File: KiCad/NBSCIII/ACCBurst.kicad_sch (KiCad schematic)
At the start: 56 parts, among them Q901 BC337-25, Q902 BC337-25, Q903 BC337-25, Q910 BC337-25, Q911 BC337-25, Q912 BC337-25, U1 LM324N

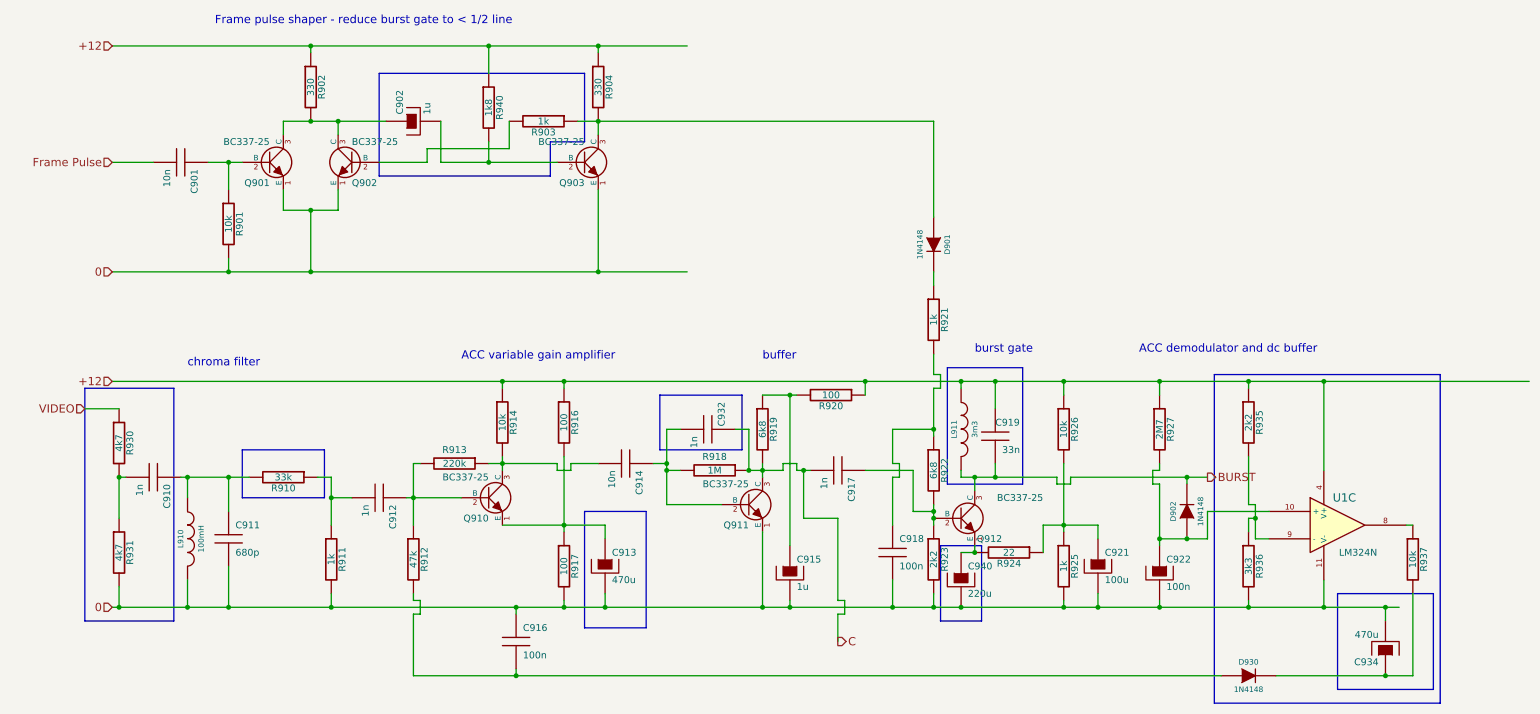
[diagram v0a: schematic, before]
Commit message: unrescue to Device:C
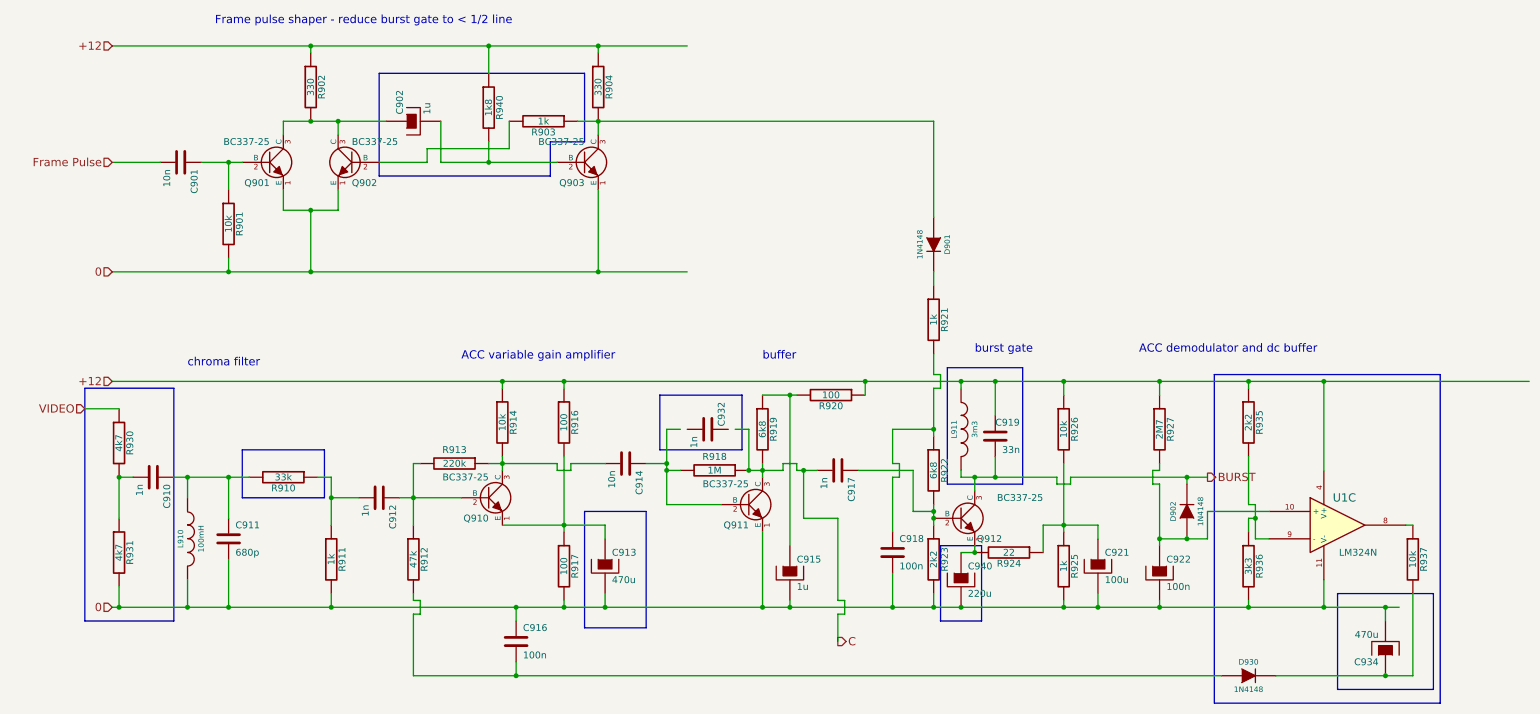
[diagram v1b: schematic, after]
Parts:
- C901, C910, C911, C912, C914, C916, C917, C918, C919, C932: symbol NBSCIII-rescue:C -> Device:C
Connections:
- net C: no longer C932.1
- net at C914.1, Q911.2 (B), R918.2: no longer C932.2
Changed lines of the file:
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@@
     (stroke (width 0) (type default) (color 0 0 0 0))
   )
-  (wire (pts (xy 176.53 104.14) (xy 167.64 104.14))
+  (wire (pts (xy 166.37 104.14) (xy 176.53 104.14))
     (stroke (width 0) (type default) (color 0 0 0 0))
   )
@@
     (stroke (width 0) (type default) (color 0 0 0 0))
   )
-  (wire (pts (xy 102.87 142.24) (xy 102.87 140.97))
+  (wire (pts (xy 102.87 139.7) (xy 102.87 142.24))
     (stroke (width 0) (type default) (color 0 0 0 0))
   )
@@
     (stroke (width 0) (type default) (color 0 0 0 0))
   )
-  (wire (pts (xy 72.39 109.22) (xy 68.58 109.22))
+  (wire (pts (xy 39.37 105.41) (xy 41.91 105.41))
+    (stroke (width 0) (type default) (color 0 0 0 0))
+  )
+  (wire (pts (xy 68.58 109.22) (xy 73.66 109.22))
     (stroke (width 0) (type default) (color 0 0 0 0))
   )
@@
     (stroke (width 0) (type default) (color 0 0 0 0))
   )
-  (wire (pts (xy 172.72 129.54) (xy 172.72 124.46))
-    (stroke (width 0) (type default) (color 0 0 0 0))
-  )
   (wire (pts (xy 210.82 129.54) (xy 210.82 127))
     (stroke (width 0) (type default) (color 0 0 0 0))
@@
     (stroke (width 0) (type default) (color 0 0 0 0))
   )
-  (wire (pts (xy 118.11 102.87) (xy 113.03 102.87))
+  (wire (pts (xy 113.03 102.87) (xy 119.38 102.87))
     (stroke (width 0) (type default) (color 0 0 0 0))
   )
@@
     (stroke (width 0) (type default) (color 0 0 0 0))
   )
-  (wire (pts (xy 49.53 105.41) (xy 49.53 111.76))
+  (wire (pts (xy 49.53 105.41) (xy 49.53 113.03))
     (stroke (width 0) (type default) (color 0 0 0 0))
   )
@@
     (stroke (width 0) (type default) (color 0 0 0 0))
   )
+  (wire (pts (xy 102.87 129.54) (xy 102.87 132.08))
+    (stroke (width 0) (type default) (color 0 0 0 0))
+  )
   (wire (pts (xy 118.11 67.31) (xy 134.62 67.31))
     (stroke (width 0) (type default) (color 0 0 0 0))
@@
     (stroke (width 0) (type default) (color 0 0 0 0))
   )
+  (wire (pts (xy 172.72 123.19) (xy 172.72 129.54))
+    (stroke (width 0) (type default) (color 0 0 0 0))
+  )
   (wire (pts (xy 180.34 129.54) (xy 180.34 127))
     (stroke (width 0) (type default) (color 0 0 0 0))
@@
     (stroke (width 0) (type default) (color 0 0 0 0))
   )
-  (wire (pts (xy 29.21 105.41) (xy 30.48 105.41))
+  (wire (pts (xy 29.21 105.41) (xy 31.75 105.41))
     (stroke (width 0) (type default) (color 0 0 0 0))
   )
@@
     (stroke (width 0) (type default) (color 0 0 0 0))
   )
-  (wire (pts (xy 102.87 129.54) (xy 102.87 130.81))
-    (stroke (width 0) (type default) (color 0 0 0 0))
-  )
   (polyline (pts (xy 129.54 90.17) (xy 144.78 90.17))
     (stroke (width 0) (type default) (color 0 0 0 0))
@@
     (stroke (width 0) (type default) (color 0 0 0 0))
   )
-  (wire (pts (xy 40.64 105.41) (xy 41.91 105.41))
-    (stroke (width 0) (type default) (color 0 0 0 0))
-  )
   (wire (pts (xy 110.49 104.14) (xy 110.49 102.87))
     (stroke (width 0) (type default) (color 0 0 0 0))
@@
     (stroke (width 0) (type default) (color 0 0 0 0))
   )
-  (wire (pts (xy 191.77 105.41) (xy 191.77 102.87))
+  (wire (pts (xy 191.77 101.6) (xy 191.77 105.41))
     (stroke (width 0) (type default) (color 0 0 0 0))
   )
@@
     (stroke (width 0) (type default) (color 0 0 0 0))
   )
-  (wire (pts (xy 156.21 104.14) (xy 157.48 104.14))
+  (wire (pts (xy 156.21 104.14) (xy 158.75 104.14))
     (stroke (width 0) (type default) (color 0 0 0 0))
   )
@@
     (stroke (width 0) (type default) (color 0 0 0 0))
   )
-  (wire (pts (xy 82.55 109.22) (xy 83.82 109.22))
+  (wire (pts (xy 81.28 109.22) (xy 83.82 109.22))
     (stroke (width 0) (type default) (color 0 0 0 0))
   )
@@
     (stroke (width 0) (type default) (color 0 0 0 0))
   )
-  (wire (pts (xy 172.72 105.41) (xy 172.72 114.3))
+  (wire (pts (xy 172.72 105.41) (xy 172.72 115.57))
     (stroke (width 0) (type default) (color 0 0 0 0))
   )
@@
     (stroke (width 0) (type default) (color 0 0 0 0))
   )
-  (wire (pts (xy 49.53 129.54) (xy 49.53 121.92))
+  (wire (pts (xy 49.53 120.65) (xy 49.53 129.54))
     (stroke (width 0) (type default) (color 0 0 0 0))
   )
@@
     (stroke (width 0) (type default) (color 0 0 0 0))
   )
-  (wire (pts (xy 191.77 87.63) (xy 191.77 92.71))
+  (wire (pts (xy 191.77 87.63) (xy 191.77 93.98))
     (stroke (width 0) (type default) (color 0 0 0 0))
   )
@@
     (stroke (width 0) (type default) (color 0 0 0 0))
   )
-  (wire (pts (xy 130.81 102.87) (xy 128.27 102.87))
+  (wire (pts (xy 127 102.87) (xy 130.81 102.87))
     (stroke (width 0) (type default) (color 0 0 0 0))
   )
@@
     (stroke (width 0) (type default) (color 0 0 0 0))
   )
-  (wire (pts (xy 35.56 46.99) (xy 27.94 46.99))
+  (wire (pts (xy 27.94 46.99) (xy 36.83 46.99))
     (stroke (width 0) (type default) (color 0 0 0 0))
   )
@@
     (stroke (width 0) (type default) (color 0 0 0 0))
   )
-  (wire (pts (xy 49.53 46.99) (xy 45.72 46.99))
+  (wire (pts (xy 44.45 46.99) (xy 49.53 46.99))
     (stroke (width 0) (type default) (color 0 0 0 0))
   )
@@
     (pin "2")
   )
-  (symbol (lib_id "NBSCIII-rescue:C") (at 40.64 46.99 270) (unit 1)
+  (symbol (lib_id "Device:C") (at 40.64 46.99 270) (unit 1)
     (in_bom yes) (on_board yes)
     (property "Reference" "C901" (id 0) (at 43.18 48.26 0)
@@
     (pin "2")
   )
-  (symbol (lib_id "NBSCIII-rescue:C") (at 49.53 116.84 0) (unit 1)
+  (symbol (lib_id "Device:C") (at 49.53 116.84 0) (unit 1)
     (in_bom yes) (on_board yes)
     (property "Reference" "C911" (id 0) (at 50.8 114.3 0)
@@
     (pin "2")
   )
-  (symbol (lib_id "NBSCIII-rescue:C") (at 77.47 109.22 270) (unit 1)
+  (symbol (lib_id "Device:C") (at 77.47 109.22 270) (unit 1)
     (in_bom yes) (on_board yes)
     (property "Reference" "C912" (id 0) (at 80.01 110.49 0)
@@
     (pin "2")
   )
-  (symbol (lib_id "NBSCIII-rescue:C") (at 102.87 135.89 0) (unit 1)
+  (symbol (lib_id "Device:C") (at 102.87 135.89 0) (unit 1)
     (in_bom yes) (on_board yes)
     (property "Reference" "C916" (id 0) (at 104.14 133.35 0)
@@
     (pin "2")
   )
-  (symbol (lib_id "NBSCIII-rescue:C") (at 123.19 102.87 270) (unit 1)
+  (symbol (lib_id "Device:C") (at 123.19 102.87 270) (unit 1)
     (in_bom yes) (on_board yes)
     (property "Reference" "C914" (id 0) (at 125.73 104.14 0)
@@
     (pin "2")
   )
-  (symbol (lib_id "NBSCIII-rescue:C") (at 172.72 119.38 0) (unit 1)
+  (symbol (lib_id "Device:C") (at 172.72 119.38 0) (unit 1)
     (in_bom yes) (on_board yes)
     (property "Reference" "C918" (id 0) (at 173.99 116.84 0)
@@
     (pin "2")
   )
-  (symbol (lib_id "NBSCIII-rescue:C") (at 162.56 104.14 270) (unit 1)
+  (symbol (lib_id "Device:C") (at 162.56 104.14 270) (unit 1)
     (in_bom yes) (on_board yes)
     (property "Reference" "C917" (id 0) (at 165.1 105.41 0)
@@
     (pin "2")
   )
-  (symbol (lib_id "NBSCIII-rescue:C") (at 191.77 97.79 0) (unit 1)
+  (symbol (lib_id "Device:C") (at 191.77 97.79 0) (unit 1)
     (in_bom yes) (on_board yes)
     (property "Reference" "C919" (id 0) (at 191.77 95.25 0)
@@
     (pin "2")
   )
-  (symbol (lib_id "NBSCIII-rescue:C") (at 35.56 105.41 270) (unit 1)
+  (symbol (lib_id "Device:C") (at 35.56 105.41 270) (unit 1)
     (in_bom yes) (on_board yes)
     (property "Reference" "C910" (id 0) (at 38.1 106.68 0)
@@
     (pin "2")
   )
-  (symbol (lib_id "NBSCIII-rescue:C") (at 138.43 96.52 270) (unit 1)
+  (symbol (lib_id "Device:C") (at 138.43 96.52 270) (unit 1)
     (in_bom yes) (on_board yes)
     (property "Reference" "C932" (id 0) (at 140.97 91.44 0)

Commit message: unrescue to Device:C_Polarized
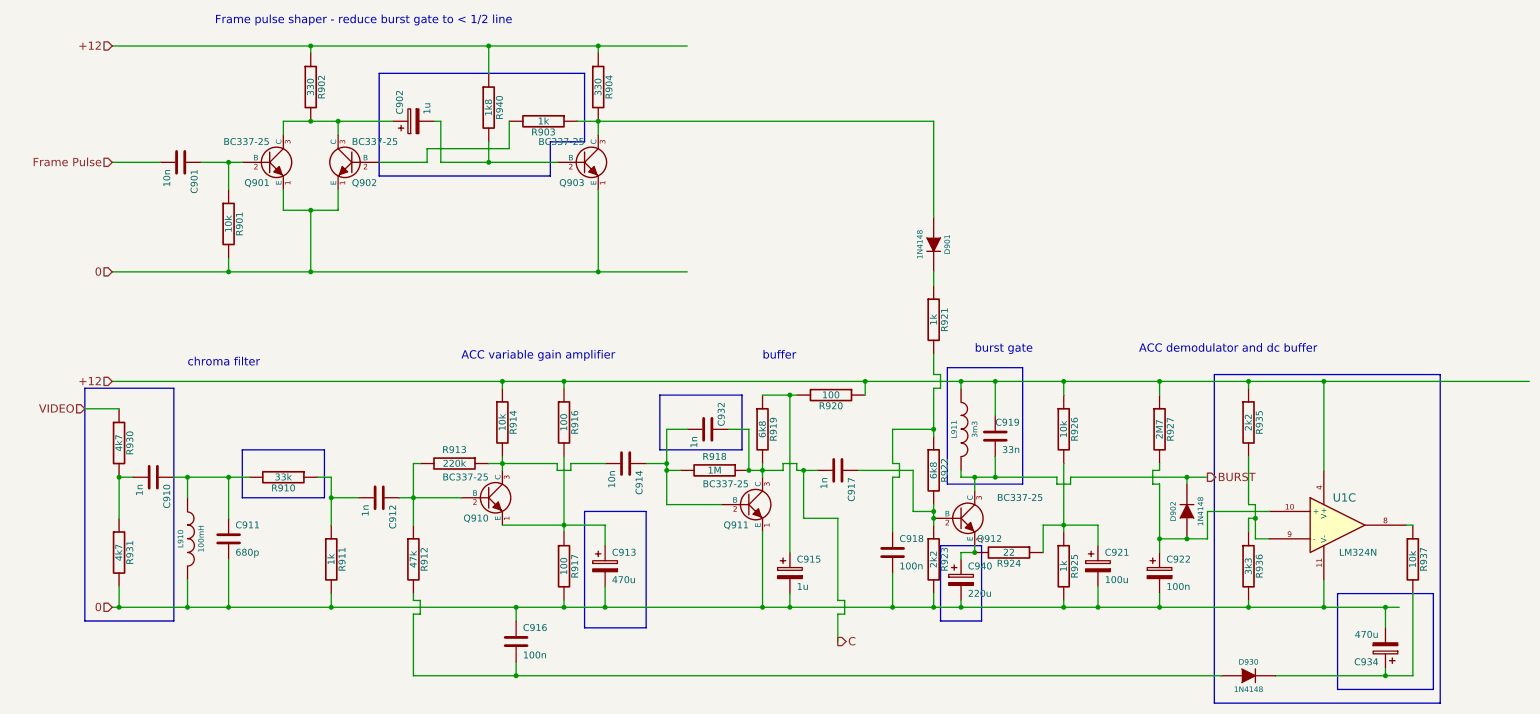
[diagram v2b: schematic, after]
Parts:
- C902, C913, C915, C921, C922, C934, C940: symbol NBSCIII-rescue:CP -> Device:C_Polarized
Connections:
- net C: now also C932.1
- net at C914.1, Q911.2 (B), R918.2: now also C932.2

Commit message: unrescue Device:R
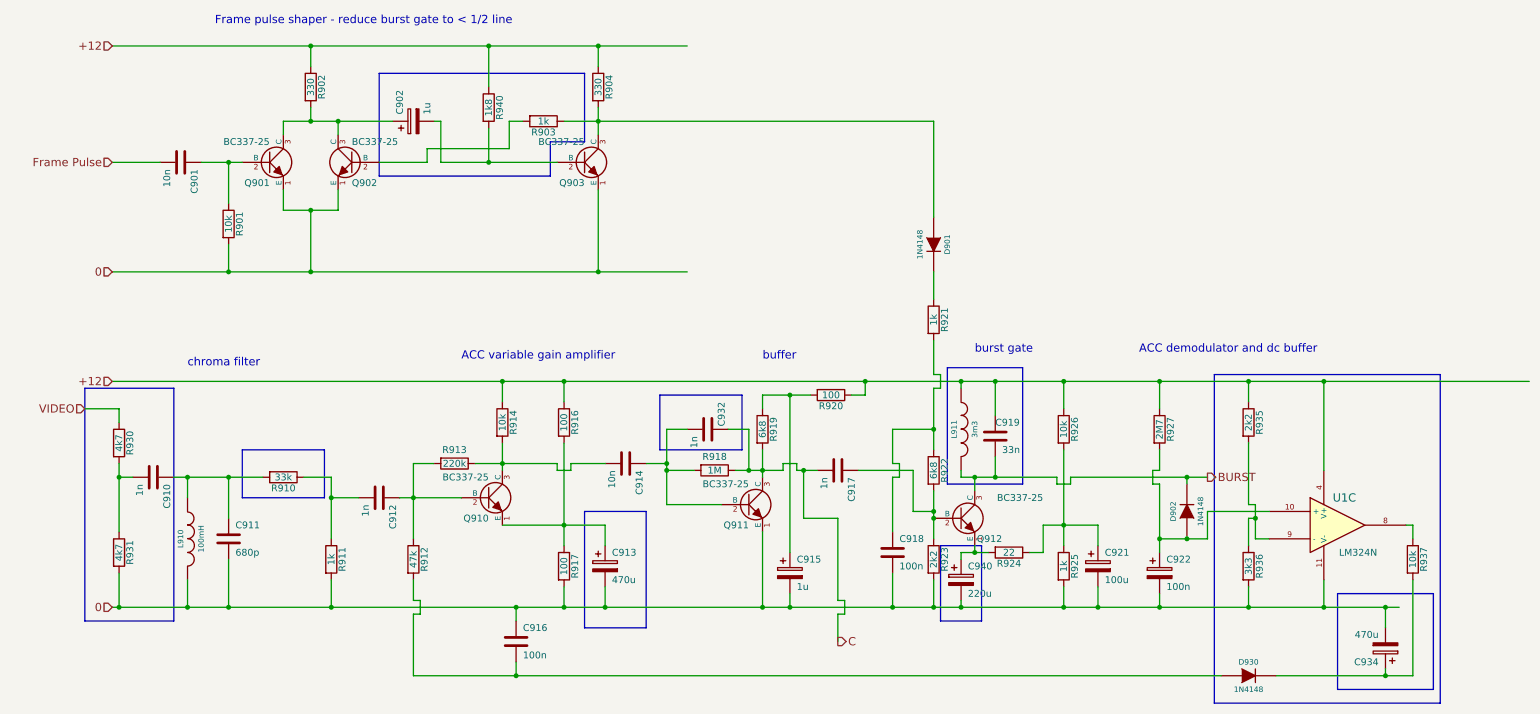
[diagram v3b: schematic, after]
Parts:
- R901, R902, R903, R904, R910, R911, R912, R913, R914, R916, R917, R918, R919, R920, R921, R922, R923, R924, R925, R926, R927, R930, R931, R935, R936, R937, R940: symbol NBSCIII-rescue:R -> Device:R

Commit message: unrescue NPN
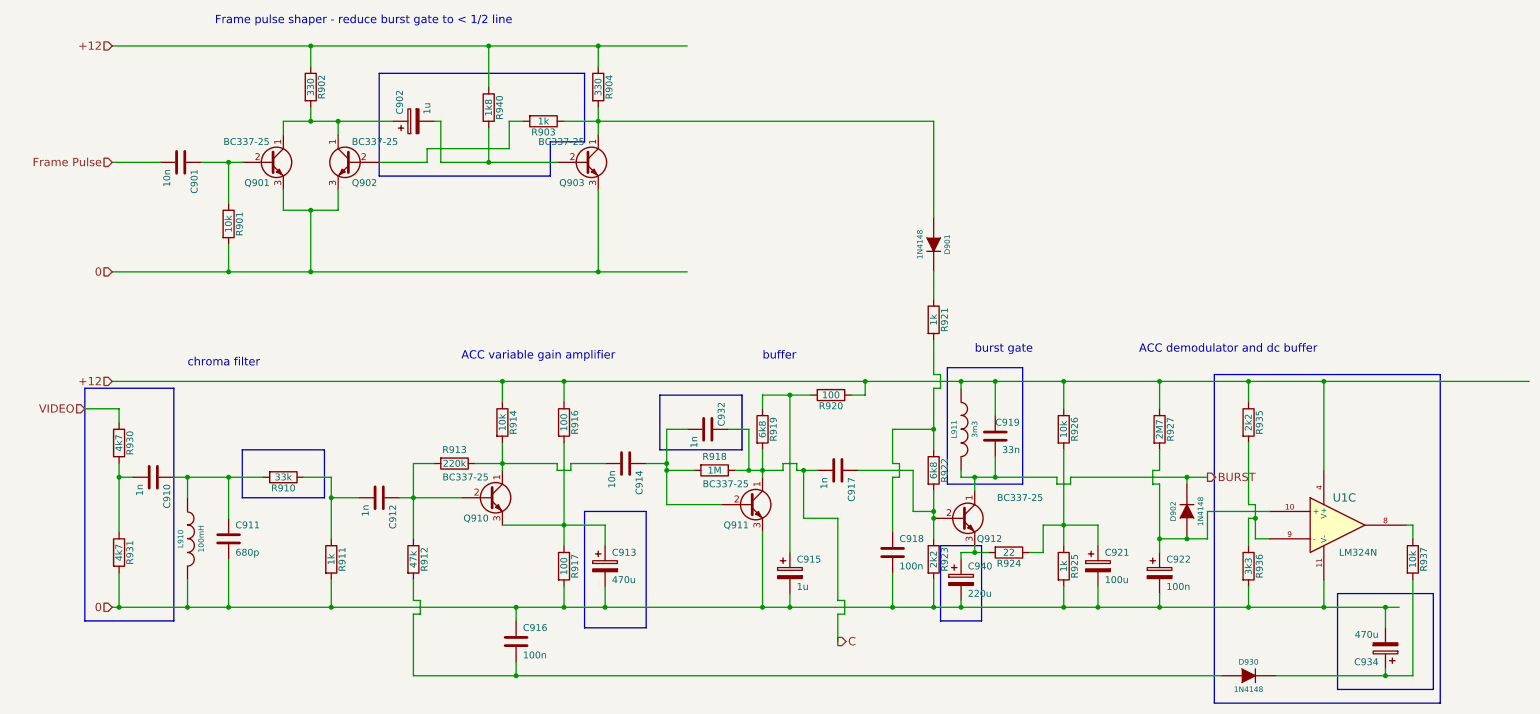
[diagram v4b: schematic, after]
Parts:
- Q901, Q902, Q903, Q910, Q911, Q912: symbol NBSCIII-rescue:NPN -> Device:Q_NPN_CBE
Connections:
- net 0: now also Q901.3 (E), Q902.3 (E), Q903.3 (E), Q911.3 (E); no longer Q901.1 (E), Q902.1 (E), Q903.1 (E), Q911.1 (E)
- net BURST: now also Q912.1 (C); no longer Q912.3 (C)
- net C: now also Q911.1 (C); no longer Q911.3 (C)
- net at C902.1, R902.2: now also Q901.1 (C), Q902.1 (C); no longer Q901.3 (C), Q902.3 (C)
- net at D901.1 (A), R903.1, R904.2: now also Q903.1 (C); no longer Q903.3 (C)
- net at C914.2, R913.1, R914.2: now also Q910.1 (C); no longer Q910.3 (C)
- net at C913.1, R916.2, R917.1: now also Q910.3 (E); no longer Q910.1 (E)
- net at C940.1, R924.2: now also Q912.3 (E); no longer Q912.1 (E)
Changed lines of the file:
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@@
     (effects (font (size 1.524 1.524)) (justify right))
   )
-  (symbol (lib_id "NBSCIII-rescue:NPN") (at 57.15 46.99 0) (unit 1)
+  (symbol (lib_id "Device:Q_NPN_CBE") (at 57.15 46.99 0) (unit 1)
     (in_bom yes) (on_board yes)
     (property "Reference" "Q901" (id 0) (at 57.15 50.8 0)
@@
     (pin "3")
   )
-  (symbol (lib_id "NBSCIII-rescue:NPN") (at 72.39 46.99 0) (mirror y) (unit 1)
+  (symbol (lib_id "Device:Q_NPN_CBE") (at 72.39 46.99 0) (mirror y) (unit 1)
     (in_bom yes) (on_board yes)
     (property "Reference" "Q902" (id 0) (at 72.39 50.8 0)
@@
     (pin "3")
   )
-  (symbol (lib_id "NBSCIII-rescue:NPN") (at 115.57 46.99 0) (unit 1)
+  (symbol (lib_id "Device:Q_NPN_CBE") (at 115.57 46.99 0) (unit 1)
     (in_bom yes) (on_board yes)
     (property "Reference" "Q903" (id 0) (at 115.57 50.8 0)
@@
     (pin "2")
   )
-  (symbol (lib_id "NBSCIII-rescue:NPN") (at 97.79 109.22 0) (unit 1)
+  (symbol (lib_id "Device:Q_NPN_CBE") (at 97.79 109.22 0) (unit 1)
     (in_bom yes) (on_board yes)
     (property "Reference" "Q910" (id 0) (at 97.79 113.03 0)
@@
     (pin "2")
   )
-  (symbol (lib_id "NBSCIII-rescue:NPN") (at 146.05 110.49 0) (unit 1)
+  (symbol (lib_id "Device:Q_NPN_CBE") (at 146.05 110.49 0) (unit 1)
     (in_bom yes) (on_board yes)
     (property "Reference" "Q911" (id 0) (at 146.05 114.3 0)
@@
     (pin "2")
   )
-  (symbol (lib_id "NBSCIII-rescue:NPN") (at 185.42 113.03 0) (unit 1)
+  (symbol (lib_id "Device:Q_NPN_CBE") (at 185.42 113.03 0) (unit 1)
     (in_bom yes) (on_board yes)
     (property "Reference" "Q912" (id 0) (at 193.04 116.84 0)
